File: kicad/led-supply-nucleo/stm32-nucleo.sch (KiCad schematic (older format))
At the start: 1 part, among them U4 NUCLEO64-F411RE

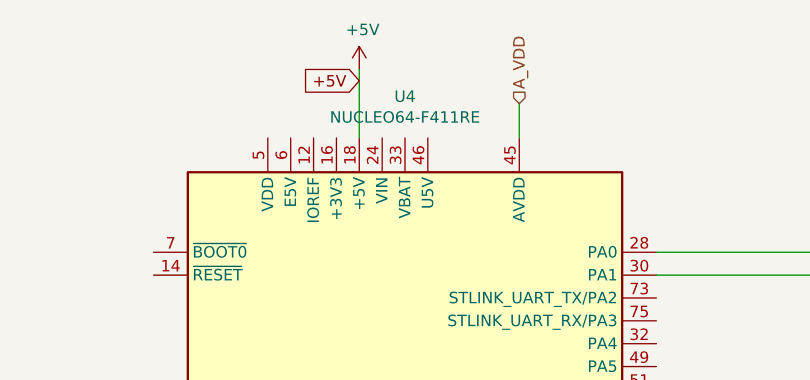
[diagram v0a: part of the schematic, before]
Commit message: Add Nucleo based board for prototyping.
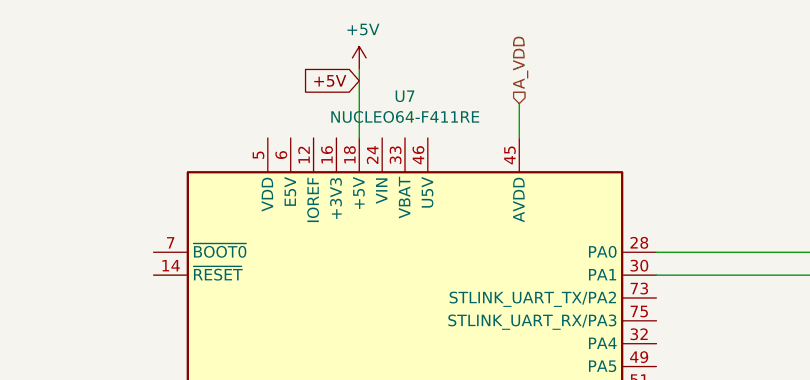
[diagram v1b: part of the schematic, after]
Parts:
- renumbered U4 to U7
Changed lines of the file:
@@
 $Descr A4 11693 8268
 encoding utf-8
-Sheet 2 3
+Sheet 3 3
 Title ""
 Date ""
@@
 $EndDescr
 $Comp
-L MCU_Module:NUCLEO64-F411RE U4
+L MCU_Module:NUCLEO64-F411RE U7
 U 1 1 6014D036
 P 3600 3000
-F 0 "U4" H 3600 5181 50  0000 C CNN
+F 0 "U7" H 3600 5181 50  0000 C CNN
 F 1 "NUCLEO64-F411RE" H 3600 5090 50  0000 C CNN
 F 2 "Module:ST_Morpho_Connector_144_STLink" H 4150 1100 50  0001 L CNN
@@
 	2500 3600 1400 3600
 $Comp
-L power:GND #PWR021
+L power:GND #PWR027
 U 1 1 601E5FBD
 P 3100 5200
-F 0 "#PWR021" H 3100 4950 50  0001 C CNN
+F 0 "#PWR027" H 3100 4950 50  0001 C CNN
 F 1 "GND" H 3105 5027 50  0000 C CNN
 F 2 "" H 3100 5200 50  0001 C CNN
@@
 	4100 1000 4100 850
 $Comp
-L power:GNDA #PWR023
+L power:GNDA #PWR029
 U 1 1 601E9DF1
 P 4100 5200
-F 0 "#PWR023" H 4100 4950 50  0001 C CNN
+F 0 "#PWR029" H 4100 4950 50  0001 C CNN
 F 1 "GNDA" H 4105 5027 50  0000 C CNN
 F 2 "" H 4100 5200 50  0001 C CNN
@@
 GNDA
 $Comp
-L power:+5V #PWR022
+L power:+5V #PWR028
 U 1 1 601EA91E
 P 3400 700
-F 0 "#PWR022" H 3400 550 50  0001 C CNN
+F 0 "#PWR028" H 3400 550 50  0001 C CNN
 F 1 "+5V" H 3415 873 50  0000 C CNN
 F 2 "" H 3400 700 50  0001 C CNN
